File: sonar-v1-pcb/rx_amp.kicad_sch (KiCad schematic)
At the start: 7 parts, among them U2 ${SIM.PARAMS}, U28 ${SIM.PARAMS}

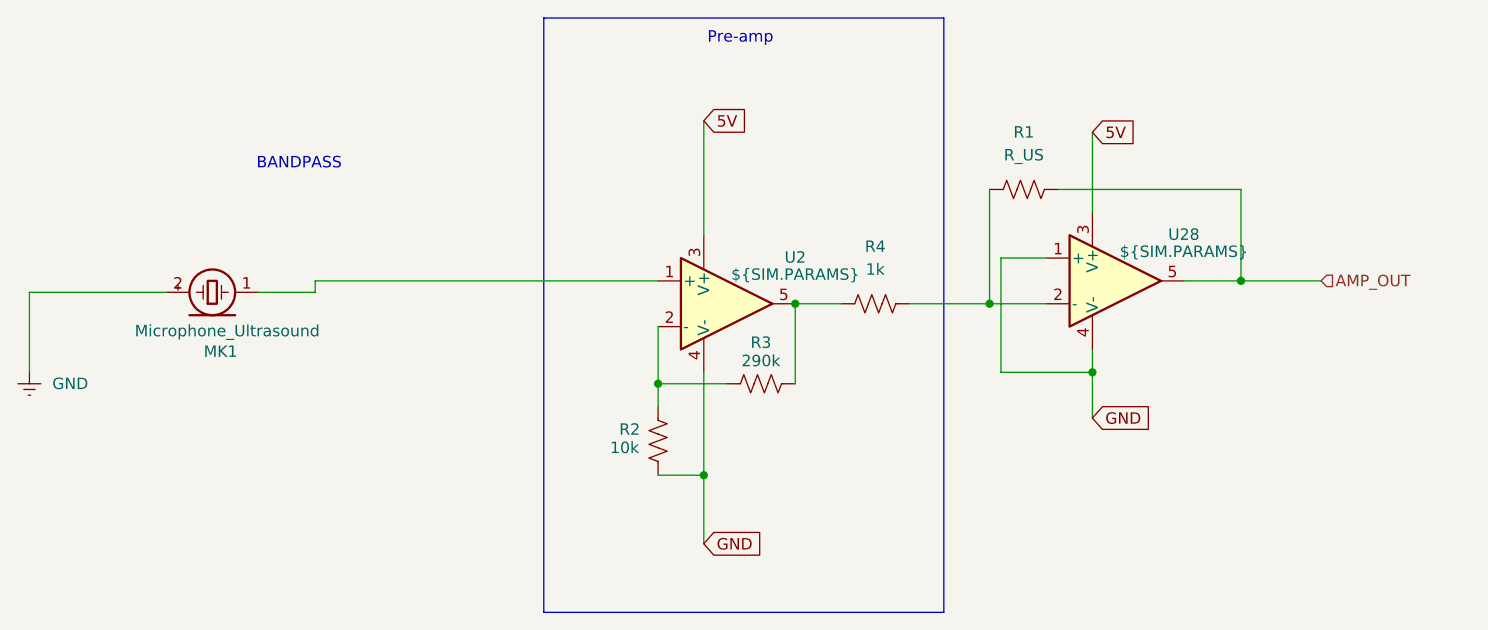
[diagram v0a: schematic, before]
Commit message: Update gitignore and save schematic/PCB progress
Co-Authored-By: Claude Opus 4.6 <noreply@anthropic.com>
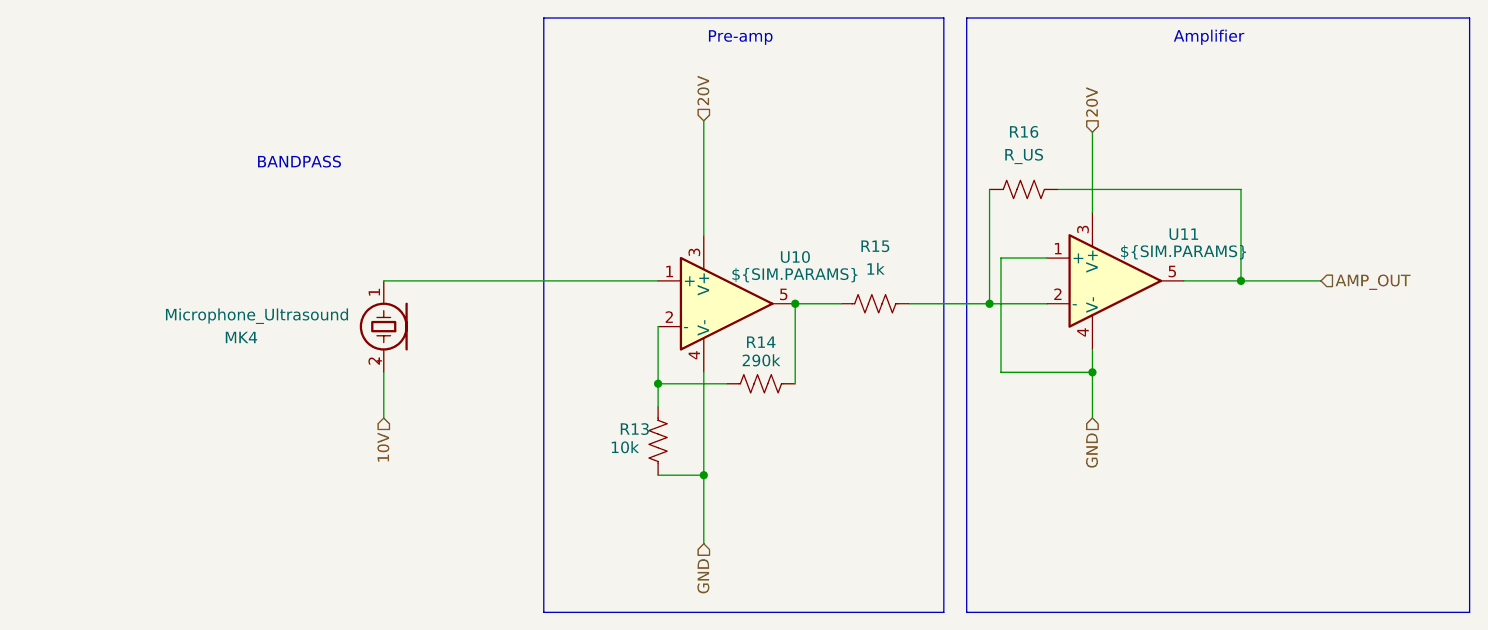
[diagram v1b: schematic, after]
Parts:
- R13: renamed from R2; footprint Resistor_SMD:R_0402_1005Metric -> Capacitor_SMD:C_0201_0603Metric
- R14: renamed from R3; footprint Resistor_SMD:R_0402_1005Metric -> Capacitor_SMD:C_0201_0603Metric
- R15: renamed from R4; footprint Resistor_SMD:R_0402_1005Metric -> Capacitor_SMD:C_0201_0603Metric
- renumbered MK1 to MK4, R1 to R16, U2 to U10, U28 to U11
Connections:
- net GND: no longer MK4.2 (+)
- net 5V renamed 20V
- new net 10V: MK4.2 (+)
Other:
- note added: "Amplifier"
- moved on the sheet: MK4
